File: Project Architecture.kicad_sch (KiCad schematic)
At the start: 0 parts

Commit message: First Draft
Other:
- removed sheet Section A - Title A
- removed sheet Section B - Title B
- added sheet Connectors (connectors.kicad_sch)
- added sheet Inertial Measurement Unit (IMU.kicad_sch)
- added sheet Microcontroller (MCU.kicad_sch)
- added sheet Power (power.kicad_sch)
- note removed: "Page 4"
- note removed: "Page 5"

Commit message: Finished system overview
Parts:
- added J1, J2: SM06B-SRSS-TB_LF__SN_, KSE_connector:JST_SM06B-SRSS-TB_LF__SN_, symbol KSE_connectors:SM06B-SRSS-TB_LF__SN_
- added J4: SM08B-SRSS-TB_LF__SN_, KSE_connector:JST_SM08B-SRSS-TB_LF__SN_, symbol KSE_connectors:SM08B-SRSS-TB_LF__SN_
- added J6: UJ20-C-H-G-SMT-1-P16-TR, KSE_connector:SAMESKY_UJ20-C-H-G-SMT-1-P16-TR, symbol KSE_connectors:UJ20-C-H-G-SMT-1-P16-TR
- added Q2: SS8050, Package_TO_SOT_SMD:SOT-23, symbol Transistor_BJT:SS8050
- added R1: 75k, Resistor_SMD:R_0603_1608Metric_Pad0.98x0.95mm_HandSolder, symbol Device:R_Small
- added R10, R7: 4.7k, Resistor_SMD:R_0603_1608Metric_Pad0.98x0.95mm_HandSolder, symbol Device:R_Small
- added R15, R9: 5.1k, Resistor_SMD:R_0805_2012Metric_Pad1.20x1.40mm_HandSolder, symbol Device:R
- added R2, R3: 10k, Resistor_SMD:R_0603_1608Metric_Pad0.98x0.95mm_HandSolder, symbol Device:R_Small
- added R4: 1k, Resistor_SMD:R_0603_1608Metric_Pad0.98x0.95mm_HandSolder, symbol Device:R_Small
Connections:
- new net: Q2.1 (B), R4.1
- new net +3.3V: R3.1
- new net +3V3: J2.2
- new net +9V: J1.1
- new net +VBAT: J4.2, R1.2
- new net AGND: R2.1
- new net ANA_ADC_CURR: J4.7
- new net ANA_ADC_VBAT: R1.1, R2.2
- new net DGND: J1.5, J2.1, J2.S1 (SHIELD), J2.S2 (SHIELD), Q2.2 (E), R10.2, R7.2
- new net ESC_SIG_M1: J4.3
- new net ESC_SIG_M2: J4.4
- new net ESC_SIG_M3: J4.6
- new net ESC_SIG_M4: J4.5
- new net I2C1_SCL: J2.5, R10.1
- new net I2C1_SDA: J2.6, R7.1
- new net PGND: J1.2, J1.S1 (SHIELD), J1.S2 (SHIELD), J4.1, J6.A1_B12 (GND), J6.B1_A12 (GND), J6.SH1 (SHIELD), J6.SH2 (SHIELD), J6.SH3 (SHIELD), J6.SH4 (SHIELD), R15.2, R9.2
- new net SBUS_TX: J1.6, R4.2
- new net UART1_RX: J4.8
- new net UART2_RX: Q2.3 (C), R3.2
- new net UART4_RX: J1.4
- new net UART4_TX: J1.3
- new net UART5_RX: J2.3
- new net UART5_TX: J2.4
- new net USB_+DATA: J6.A6 (DP1), J6.B6 (DP2)
- new net USB_-DATA: J6.A7 (DN1), J6.B7 (DN2)
- new net USB_CC1: J6.A5 (CC1), R9.1
- new net USB_CC2: J6.B5 (CC2), R15.1
- new net V_USB: J6.A4_B9 (VBUS), J6.B4_A9 (VBUS)
- no-connect marks 0 -> 2
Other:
- removed sheet Connectors
- sheet Inertial Measurement Unit ports: added +3V3, DGND, IMU_CS, IMU_EXTI, {SPI1}; removed none
- sheet Microcontroller ports: added IMU_CS, IMU_EXTI, USB_+DATA, USB_-DATA, {I2C1}; removed FLASH_CS, GYRO_1_CS, GYRO_1_EXTI, I2C1_SCL, I2C1_SDA, PINIO1, SPI2_SCK, SPI2_SDI, SPI2_SDO, SPI3_SCK, SPI3_SDI, SPI3_SDO, UART1_TX, UART2_TX, UART3_RX, UART3_TX, UART6_RX, UART6_TX
- sheet Power ports: added +3V3, +9V, DGND, PGND, V_BAT, V_USB; removed none
- note added: "3A Sink"
- note added: "DESIGN NOTE: ESC "SIG" can be: - DSHOT - Multishot - Oneshot - PWM"
- note added: "DESIGN NOTE: Volage divider ratio: 11.77 : 1"
- note added: "ESC Interface (4-in-1 Betaflight)"
- note added: "IMU"
- note added: "MCU"
- note added: "NAV Interface (INAV GPS+MAG)"
- note added: "POWER"
- note added: "SBUS to UART inverter"
- note added: "USB-C INTERFACE (USB 2.0, 5V, 3A)"
- note added: "VTX Interface (DJI 04 AIR)"

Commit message: First schematic draft complete
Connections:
- net +3V3: now also J2.4; no longer J2.2
- net DGND: now also J2.3; no longer J2.1
- net UART5_RX: now also J2.1; no longer J2.3
- net UART5_TX: now also J2.2; no longer J2.4

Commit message: Layout half-way done.
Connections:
- net +3V3: now also R10.2, R7.2
- net DGND: no longer R10.2, R7.2
- net I2C1_SCL: now also R7.1; no longer R10.1
- net I2C1_SDA: now also R10.1; no longer R7.1
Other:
- moved on the sheet: R10, R7

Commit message: Initial Wiring Complete
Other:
- sheet Inertial Measurement Unit ports: added IMU_SPI_SCK, IMU_SPI_SDI, IMU_SPI_SDO; removed {SPI1}
- sheet Microcontroller ports: added MCU_I2C1_SCL, MCU_I2C1_SDA, MCU_SPI1_SCK, MCU_SPI1_SDI, MCU_SPI1_SDO; removed {I2C1}, {SPI1}

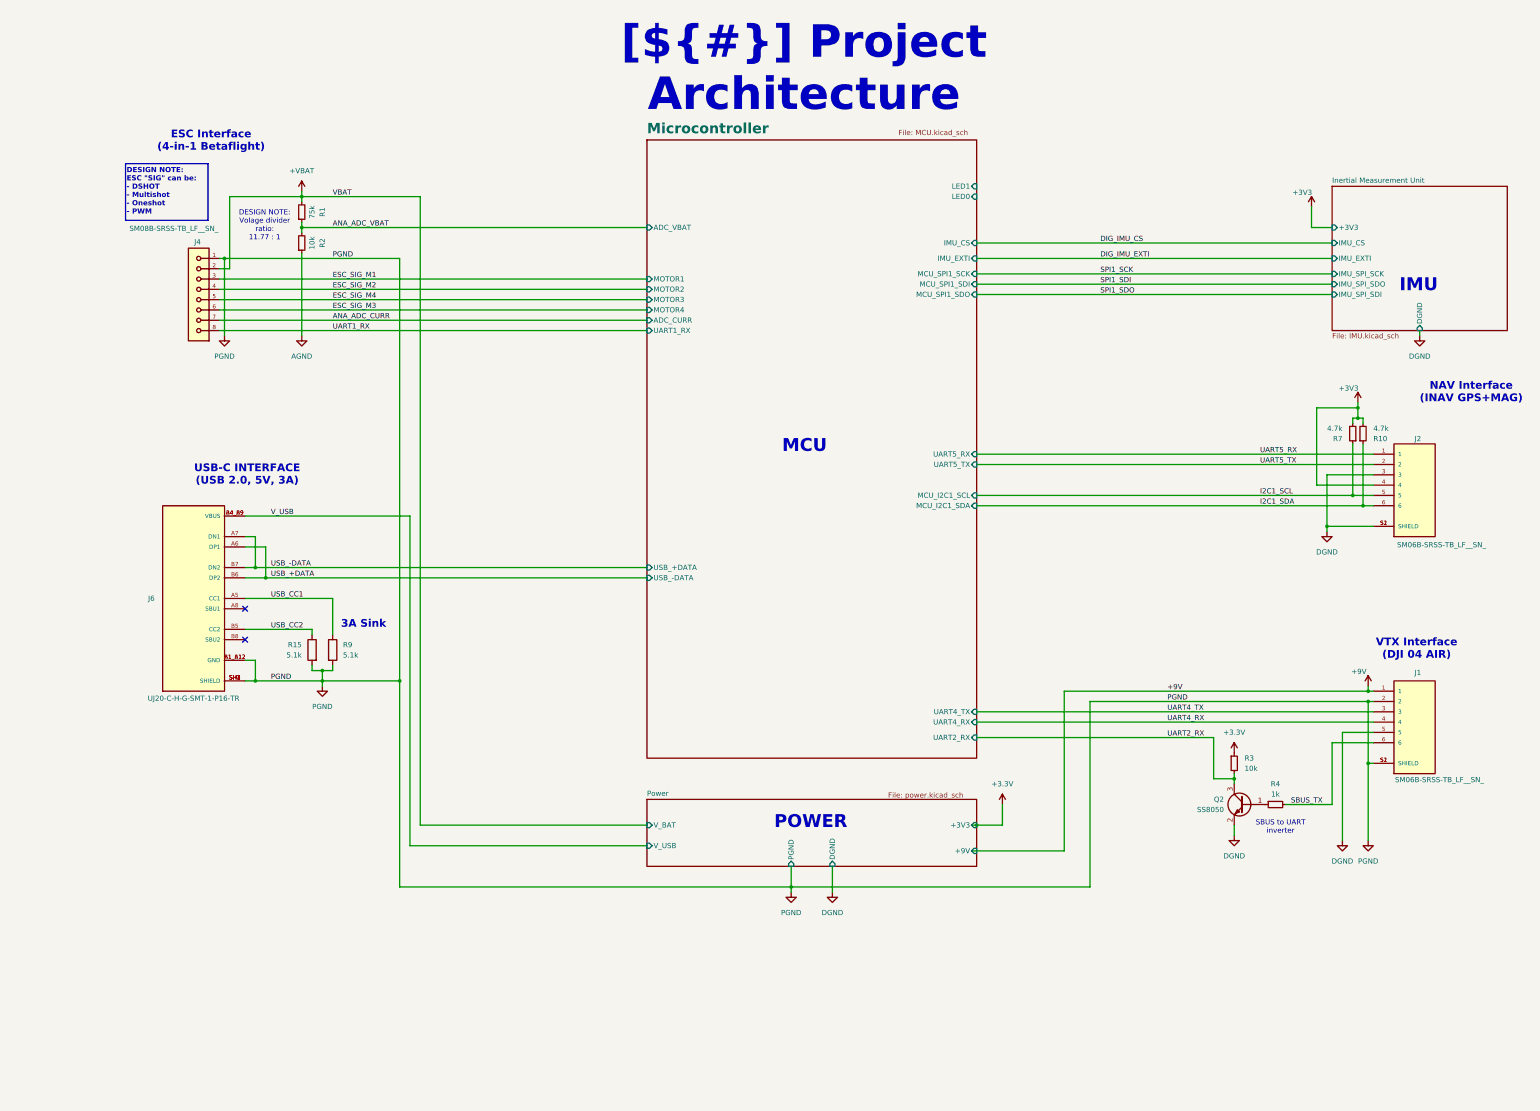
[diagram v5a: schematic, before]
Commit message: Wiring Complete, ERC and DRC remaining
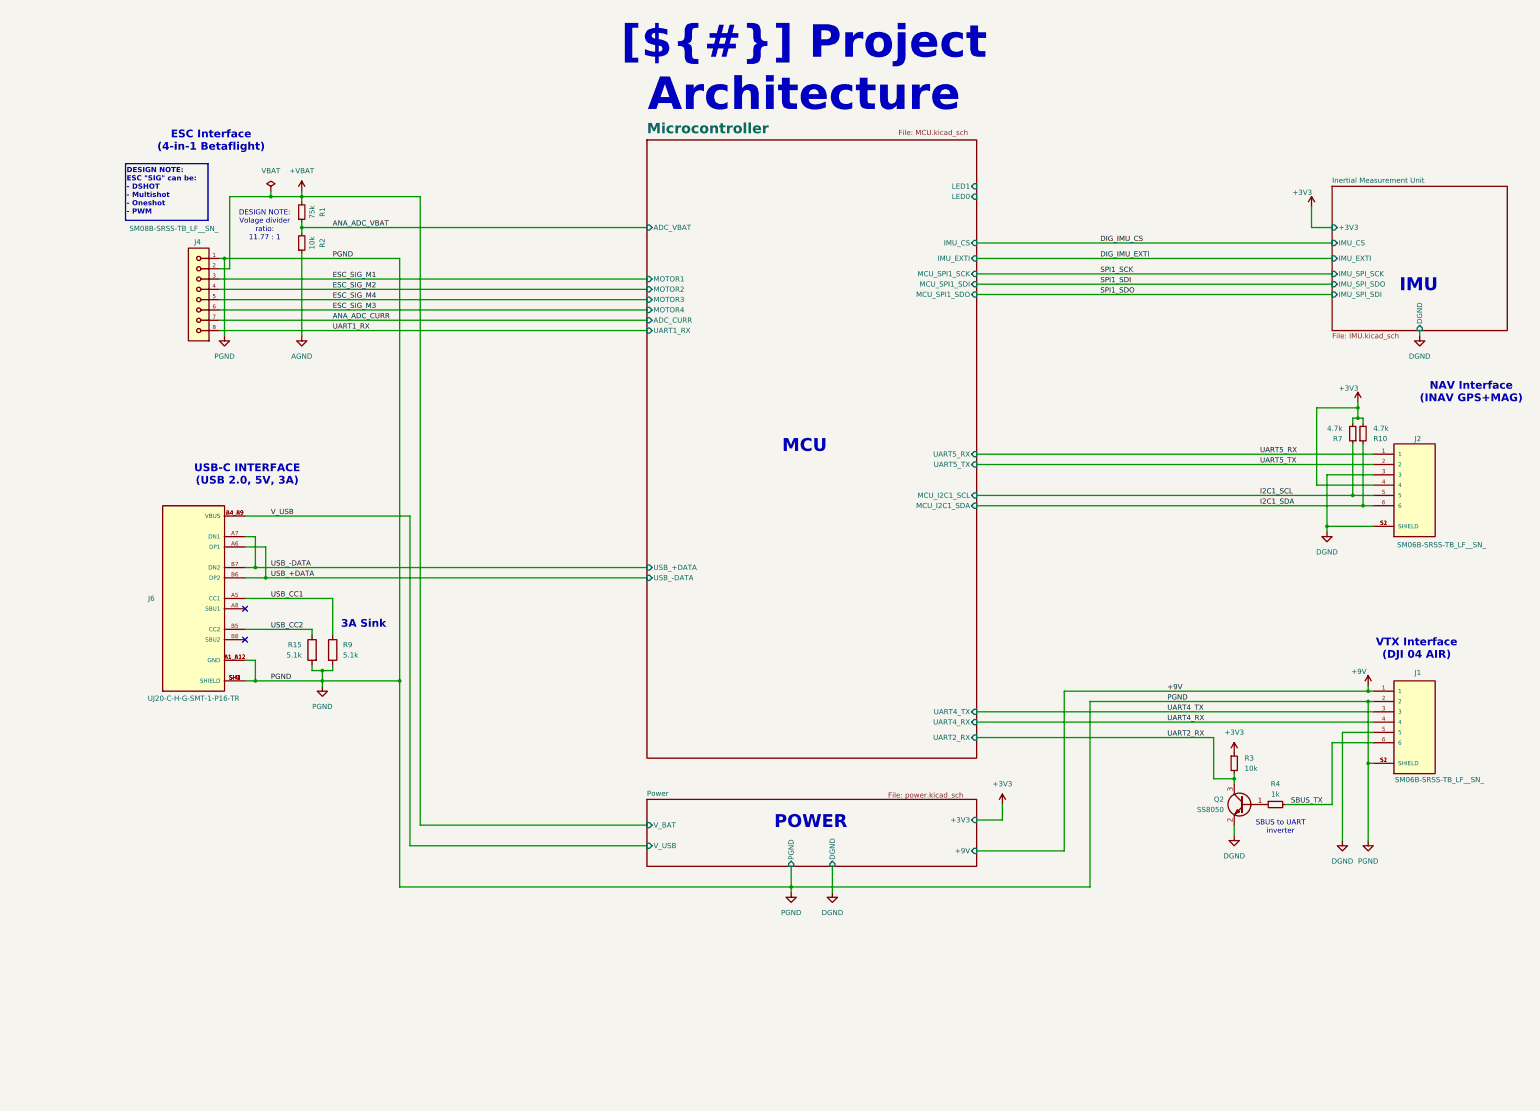
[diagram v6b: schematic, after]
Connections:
- net +3.3V is gone; now on net +3V3: R3.1

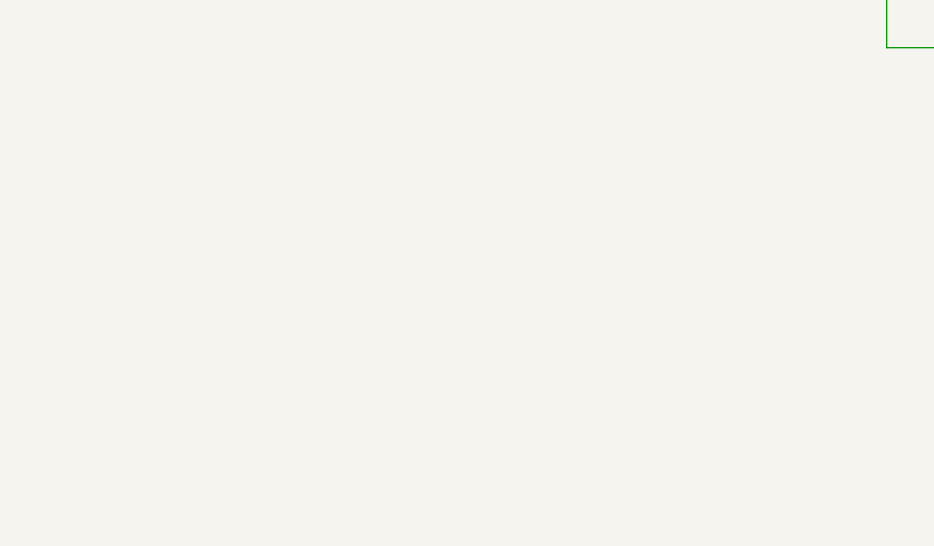
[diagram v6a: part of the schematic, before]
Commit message: Updated LDO with new component standard.
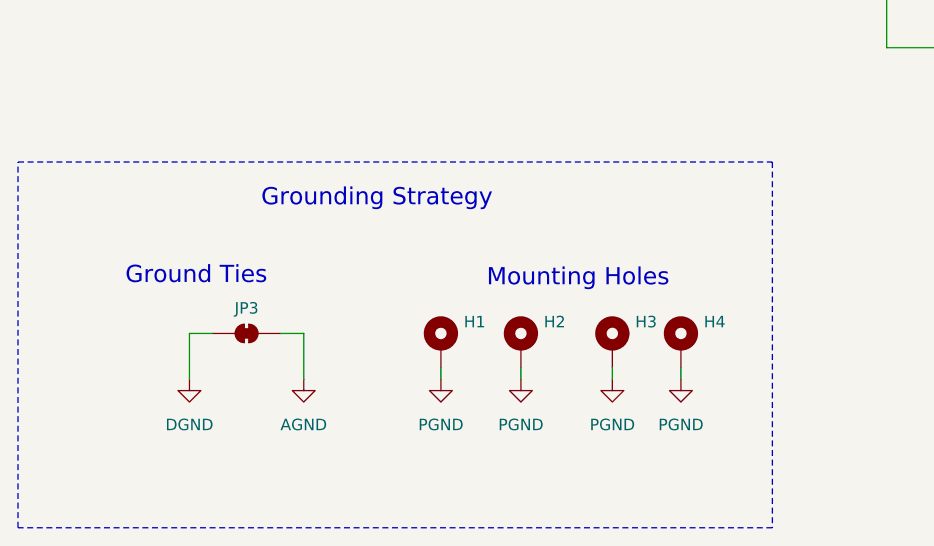
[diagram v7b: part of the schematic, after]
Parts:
- added H1, H2, H3, H4: MountingHole_Pad_MP, MountingHole:MountingHole_3.2mm_M3_DIN965_Pad, symbol Mechanical:MountingHole_Pad_MP
- added JP3: SolderJumper_2_Bridged, Jumper:SolderJumper-2_P1.3mm_Bridged2Bar_Pad1.0x1.5mm, symbol Jumper:SolderJumper_2_Bridged
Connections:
- net AGND: now also JP3.2 (B)
- net DGND: now also JP3.1 (A)
- net PGND: now also H1.MP, H2.MP, H3.MP, H4.MP
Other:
- note added: "Ground Ties"
- note added: "Grounding Strategy"
- note added: "Mounting Holes"

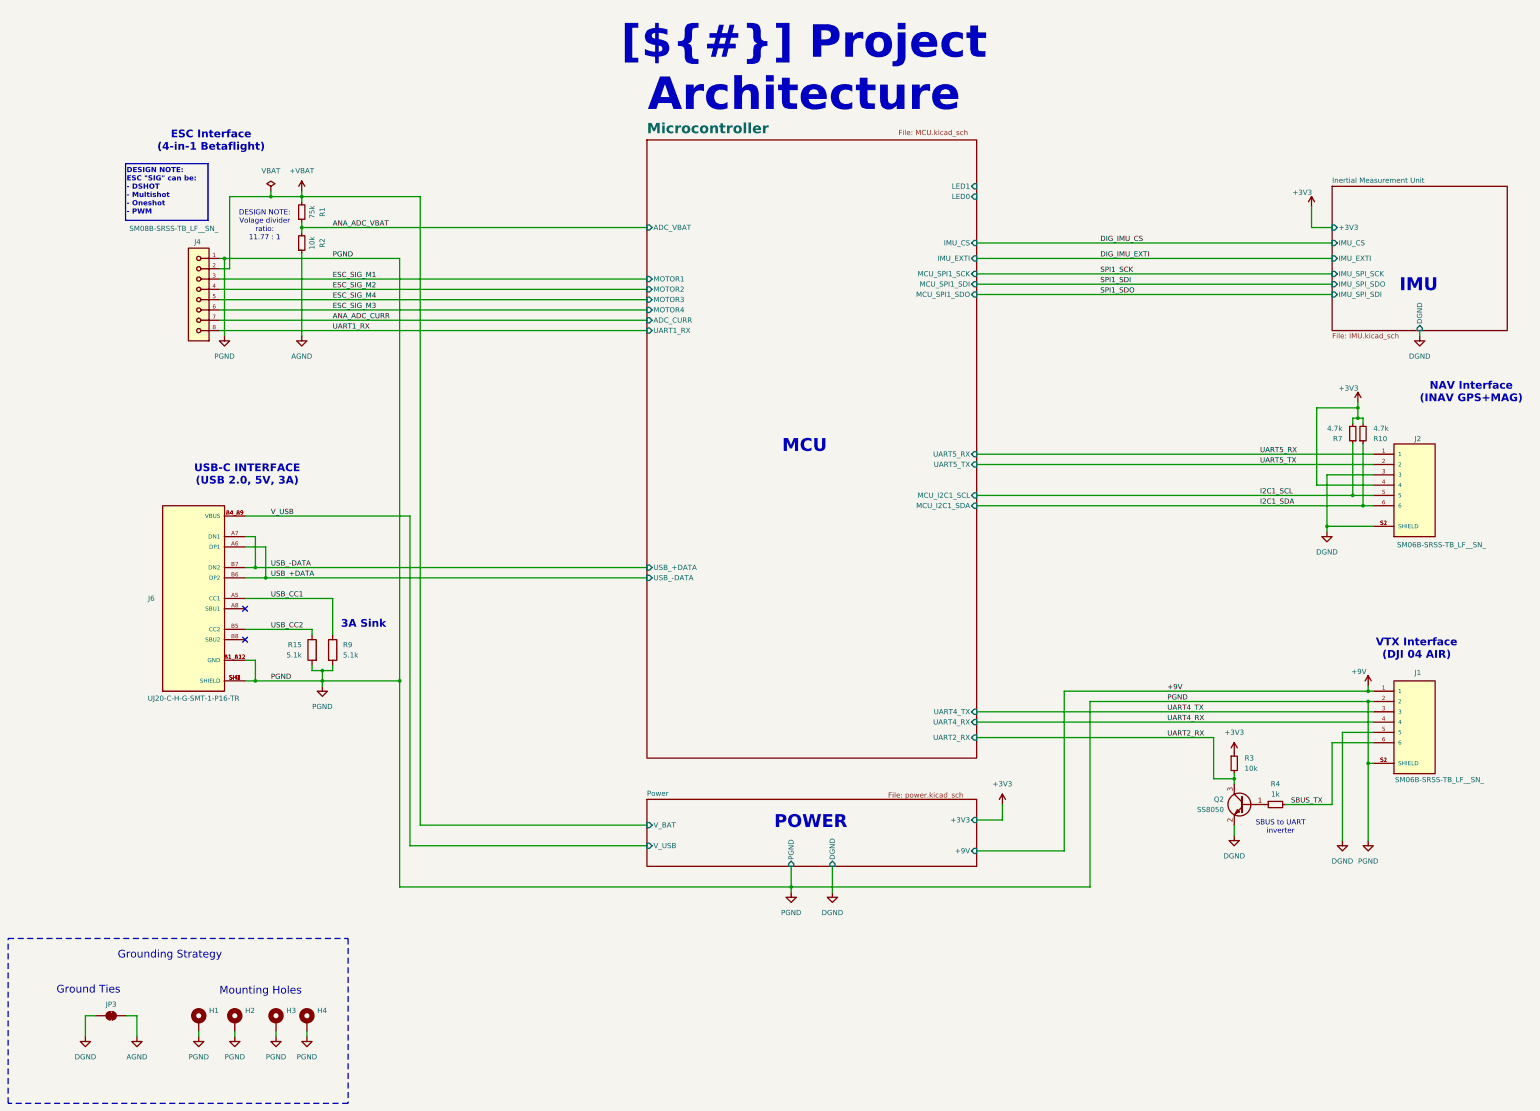
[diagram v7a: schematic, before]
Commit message: Added part-numbers and updated symbols
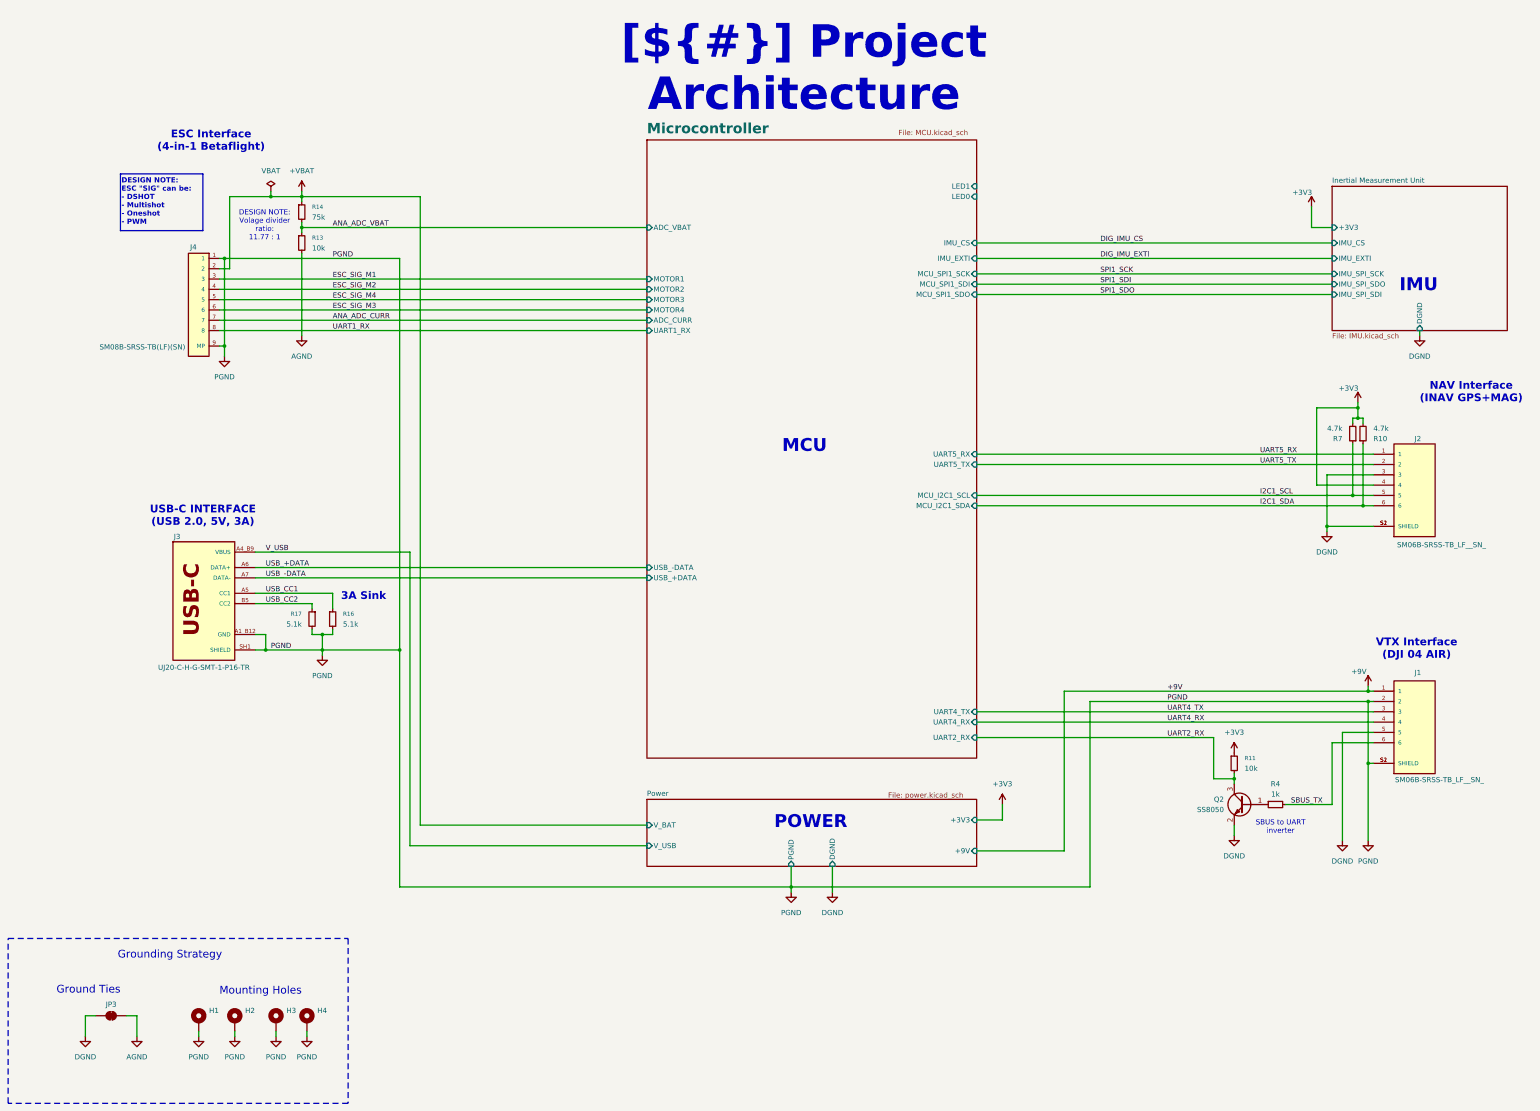
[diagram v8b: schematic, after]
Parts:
- removed J4: SM08B-SRSS-TB_LF__SN_, KSE_connector:JST_SM08B-SRSS-TB_LF__SN_, symbol KSE_connectors:SM08B-SRSS-TB_LF__SN_
- removed J6: UJ20-C-H-G-SMT-1-P16-TR, KSE_connector:SAMESKY_UJ20-C-H-G-SMT-1-P16-TR, symbol KSE_connectors:UJ20-C-H-G-SMT-1-P16-TR
- removed R1: 75k, Resistor_SMD:R_0603_1608Metric_Pad0.98x0.95mm_HandSolder, symbol Device:R_Small
- removed R15, R9: 5.1k, Resistor_SMD:R_0805_2012Metric_Pad1.20x1.40mm_HandSolder, symbol Device:R
- removed R2, R3: 10k, Resistor_SMD:R_0603_1608Metric_Pad0.98x0.95mm_HandSolder, symbol Device:R_Small
- added J3: UJ20-C-H-G-SMT-1-P16-TR, KSE_connector:SAMESKY_UJ20-C-H-G-SMT-1-P16-TR, symbol KSE_connectors:UJ20-C-H-G-SMT-1-P16-TR
- added J4: SM08B-SRSS-TB(LF)(SN), KSE_connector:JST_SM08B-SRSS-TB_LF__SN_, symbol KSE_connectors:SM08B-SRSS-TB(LF)(SN)
- added R11, R13: 10k, Resistor_SMD:R_0402_1005Metric, symbol KSE_Resistors:R_Small
- added R14: 75k, Resistor_SMD:R_0402_1005Metric, symbol KSE_Resistors:R_Small
- added R16, R17: 5.1k, Resistor_SMD:R_0402_1005Metric, symbol KSE_Resistors:R_Small
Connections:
- net +3V3: now also R11.1
- net +VBAT: now also J4.2, R14.1
- net AGND: now also R13.2
- net ANA_ADC_CURR: now also J4.7
- net ANA_ADC_VBAT: now also R13.1, R14.2
- net ESC_SIG_M1: now also J4.3
- net ESC_SIG_M2: now also J4.4
- net ESC_SIG_M3: now also J4.6
- net ESC_SIG_M4: now also J4.5
- net PGND: now also J3.A1_B12 (GND), J3.B1_A12 (GND), J3.SH1 (SHIELD), J3.SH2 (SHIELD), J3.SH3 (SHIELD), J3.SH4 (SHIELD), J4.1, J4.9 (MP), R16.2, R17.2
- net UART1_RX: now also J4.8
- net UART2_RX: now also R11.2
- net USB_+DATA: now also J3.A6 (DATA+), J3.B6 (DATA+)
- net USB_-DATA: now also J3.A7 (DATA-), J3.B7 (DATA-)
- net USB_CC1: now also J3.A5 (CC1), R16.1
- net USB_CC2: now also J3.B5 (CC2), R17.1
- net V_USB: now also J3.A4_B9 (VBUS), J3.B4_A9 (VBUS)
- new net: J3.A8 (SBU1), J3.B8 (SBU2)
- no-connect marks 2 -> 0
